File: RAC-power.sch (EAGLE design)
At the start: 1 part, among them IC1 MCP1640T-I_CHY

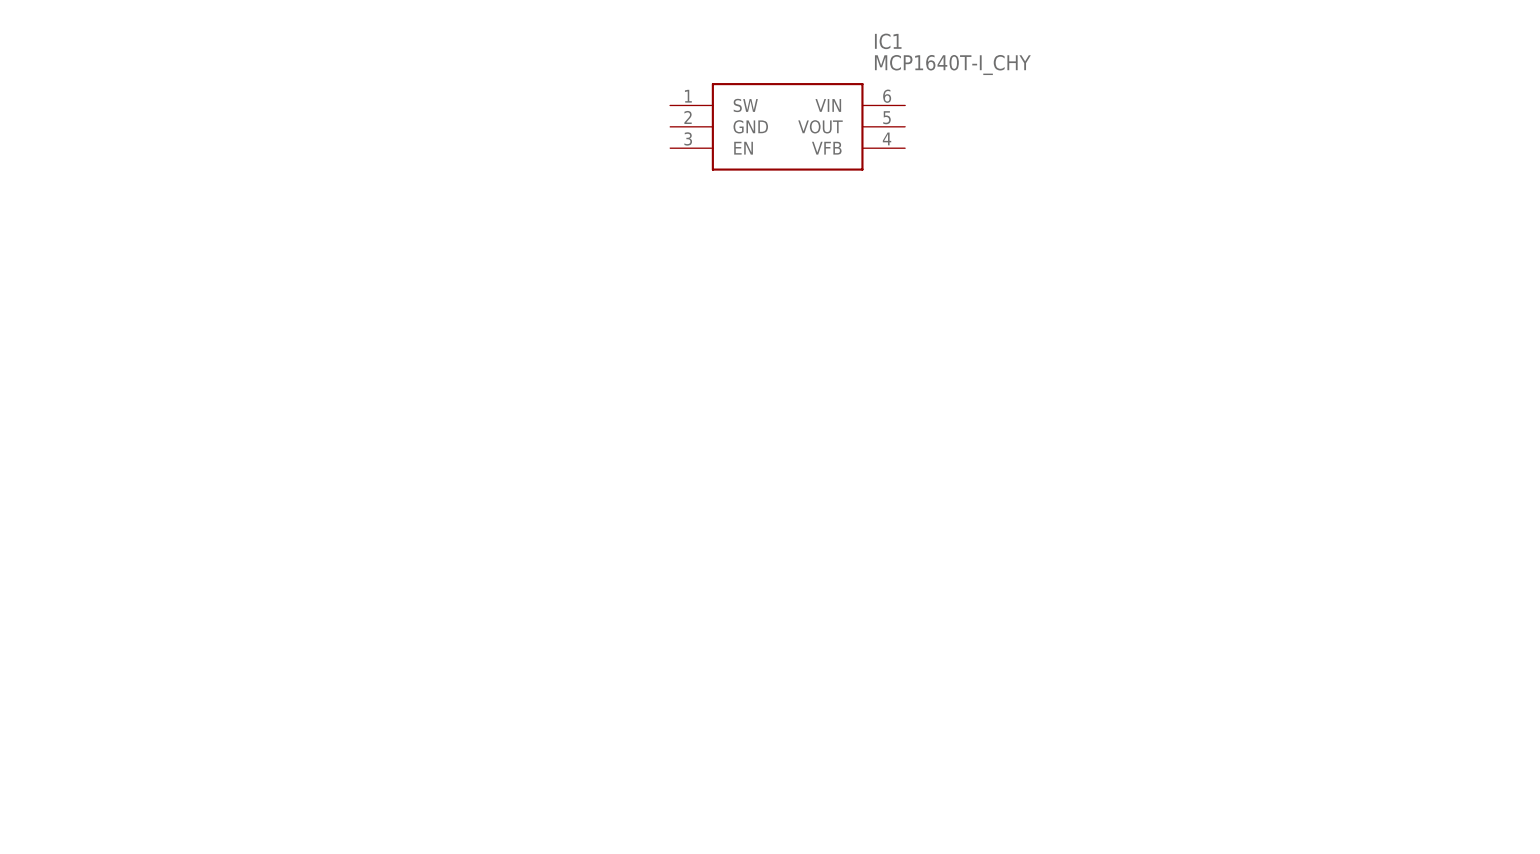
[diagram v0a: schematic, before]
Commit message: Created a basic MCP1640 boost schematic
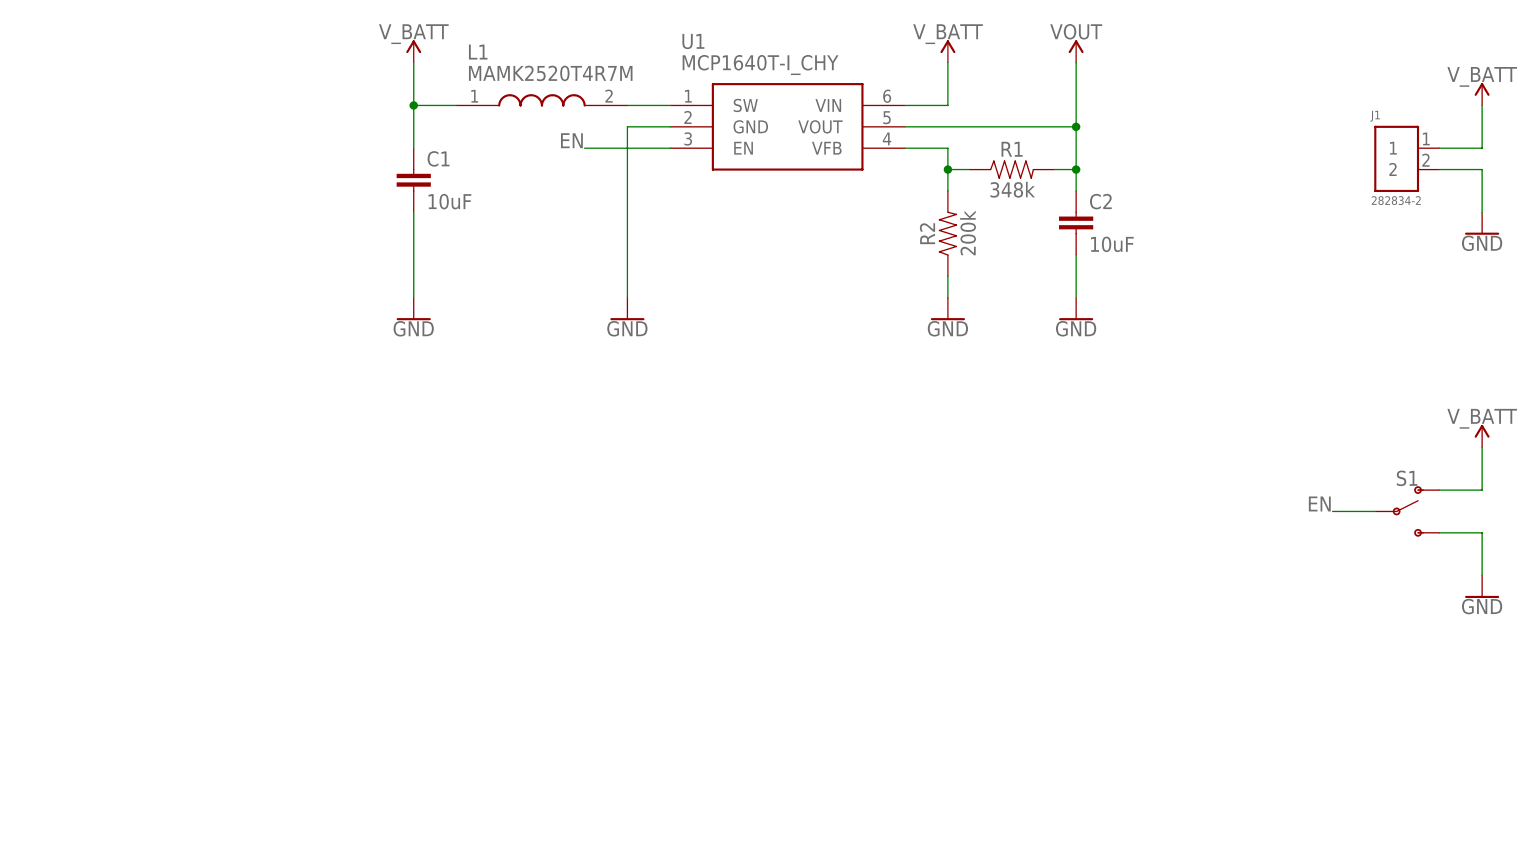
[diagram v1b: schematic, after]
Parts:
- added C1, C2: 10uF, SparkFun-Capacitors:10UF-0603-6.3V-20%
- added J1: 282834-2, RAC-Altimeter:282834-2
- added L1: MAMK2520T4R7M, RAC-Altimeter:MAMK2520T4R7M
- added R1: 348k, SparkFun-Resistors:348KOHM-0603-1/10W-1%
- added R2: 200k, SparkFun-Resistors:200KOHM-0603-1/10W-1%
- added S1: (no value), SparkFun-Switches:SWITCH-SPDT-SMD-AYZ0202
- renumbered IC1 to U1
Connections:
- new net EN: S1.P, U1.EN
- new net GND: C1.2, C2.2, J1.2, R2.1, S1.S, U1.GND
- new net N$1: L1.2, U1.SW
- new net N$2: R1.1, R2.2, U1.VFB
- new net VOUT: C2.1, R1.2, U1.VOUT
- new net V_BATT: C1.1, J1.1, L1.1, S1.O, U1.VIN

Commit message: Added battery monitor ADC, JST connector, and mounting holes
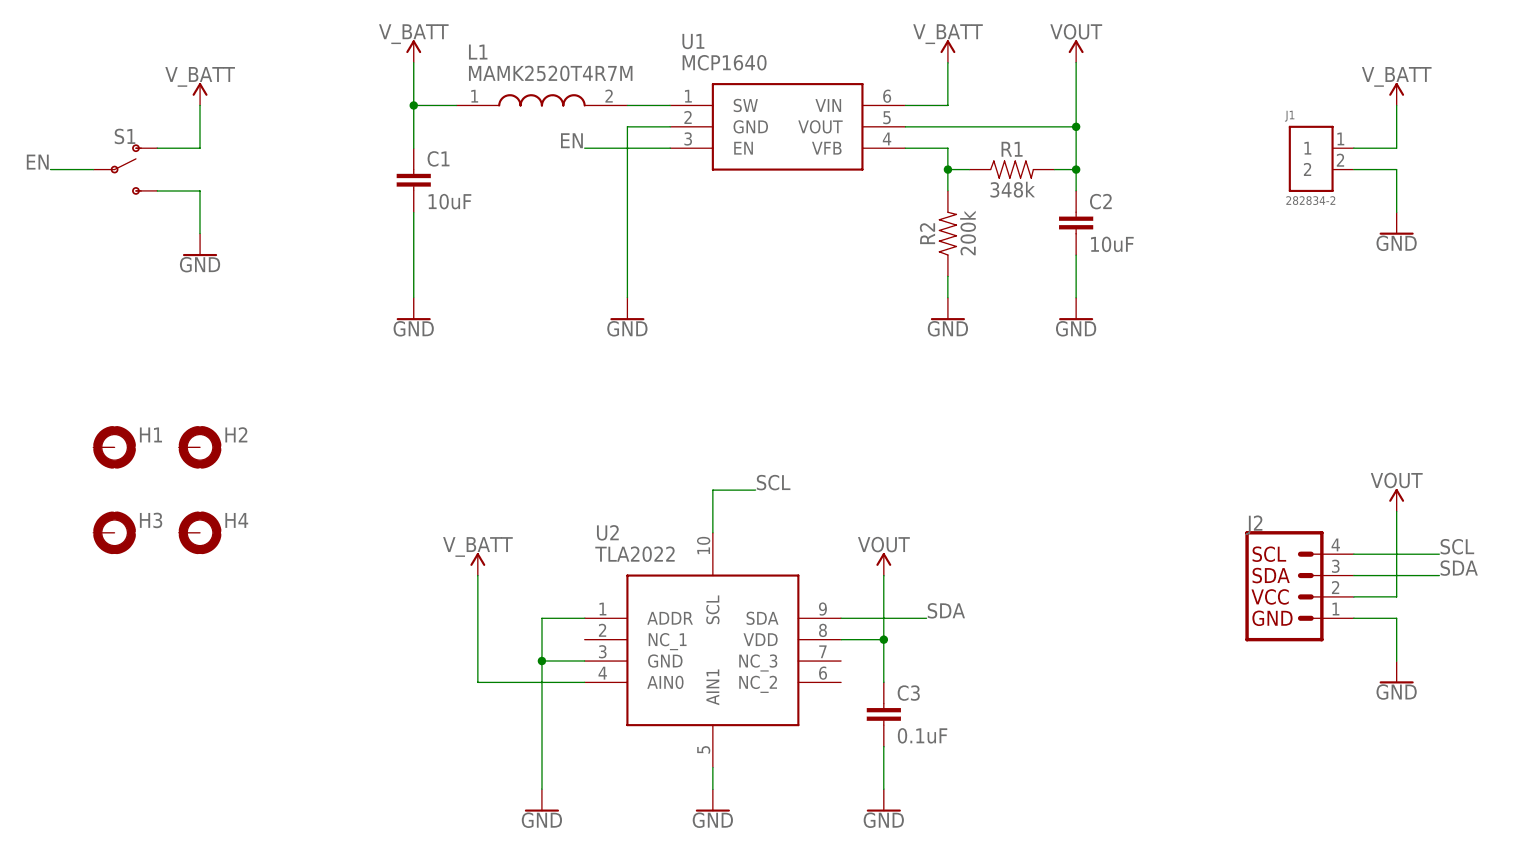
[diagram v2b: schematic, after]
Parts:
- added C3: 0.1uF, SparkFun-Capacitors:0.1UF-0603-25V-(+80/-20%)
- added H1, H2, H3, H4: MOUNT-PAD-ROUND2.8, holes:MOUNT-PAD-ROUND2.8
- added J2: (no value), SparkFun-Connectors:QWIIC_CONNECTORJS-1MM
- added U2: TLA2022, RAC-Altimeter:TLA2022IRUGR
- U1: value MCP1640T-I_CHY -> MCP1640
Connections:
- new net SCL: J2.4, U2.SCL
- new net SDA: J2.3, U2.SDA
- net GND: now also C3.2, J2.1, U2.ADDR, U2.AIN1, U2.GND
- net VOUT: now also C3.1, J2.2, U2.VDD
- net V_BATT: now also U2.AIN0
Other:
- moved on the sheet: J1, S1

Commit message: Laid out components and named some nets
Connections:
- net N$1 renamed SW
- net N$2 renamed VFB
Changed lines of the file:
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@@
 </busses>
 <nets>
-<net name="N$1" class="0">
+<net name="SW" class="0">
 <segment>
 <pinref part="U1" gate="G$1" pin="SW"/>
@@
 </segment>
 </net>
-<net name="N$2" class="0">
+<net name="VFB" class="0">
 <segment>
 <pinref part="U1" gate="G$1" pin="VFB"/>
